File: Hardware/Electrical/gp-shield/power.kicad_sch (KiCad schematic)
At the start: 38 parts, among them J1 XT60/TERM2, J2 XT60/TERM2, Q1 Q_PMOS_GDS, Q2 Q_PMOS_GDS, Q4 Q_PMOS_GDS, SW1 SW_SPDT, U1 NCP1117-5.0_SOT223, U3 LM397, U5 ADCMP350

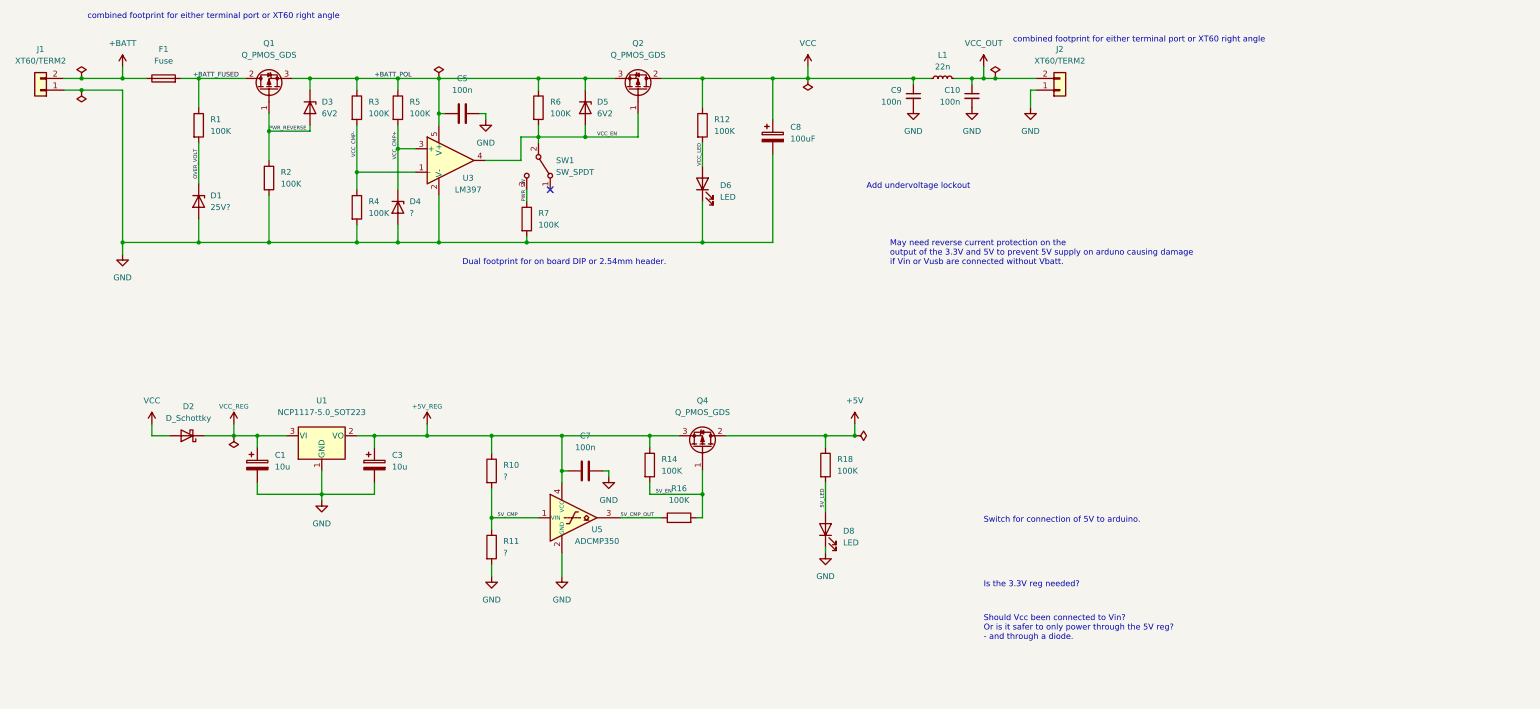
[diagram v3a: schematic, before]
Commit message: Updated Power supply design
Simplified reverse polarity and overvoltage protection
Added adjustable UVLO with precision Vref
Added hysteresis to comparators
Added precision reference to 5V cmp circuit.
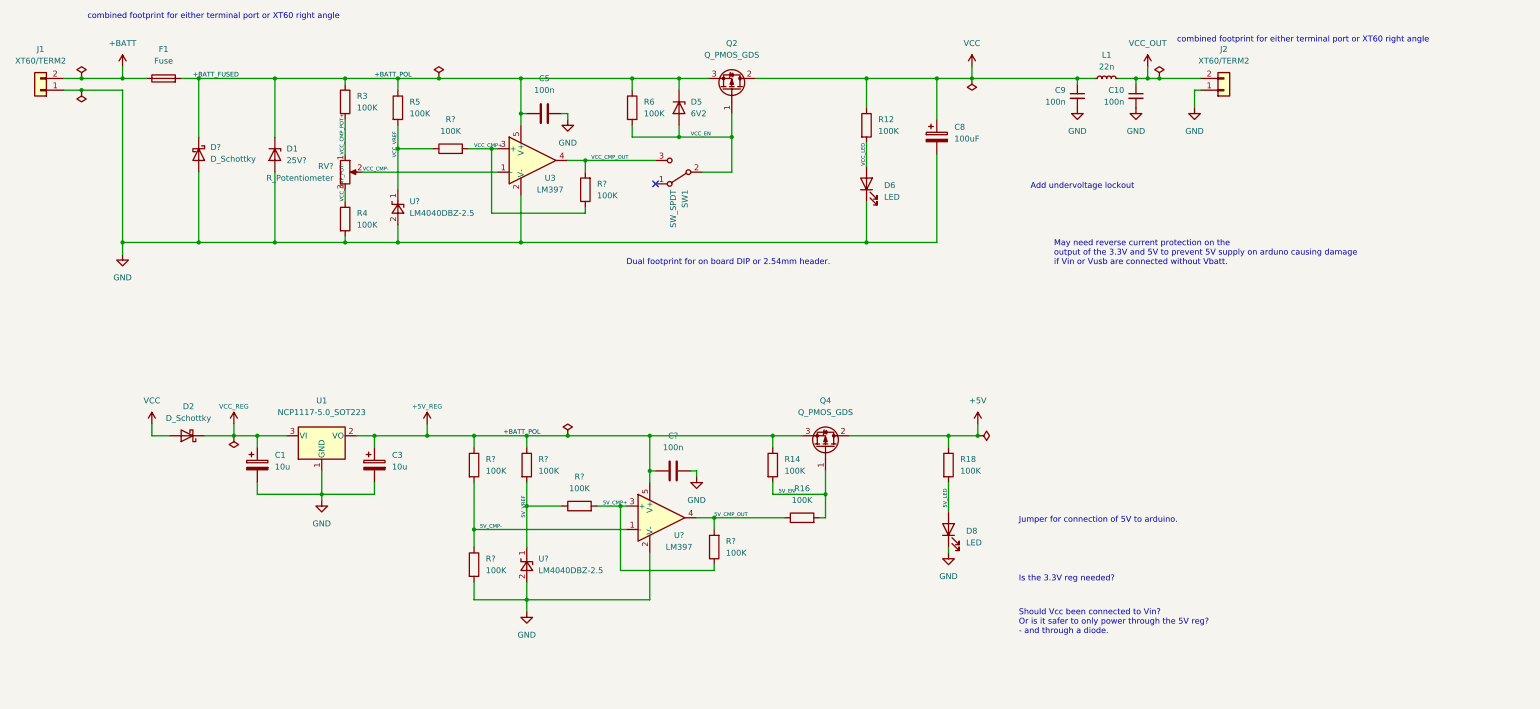
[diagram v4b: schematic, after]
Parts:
- removed C7: 100n, Capacitor_SMD:C_0805_2012Metric_Pad1.18x1.45mm_HandSolder, symbol Device:C
- removed D3: 6V2, Diode_SMD:D_0805_2012Metric_Pad1.15x1.40mm_HandSolder, symbol Device:D_Zener
- removed D4: ?, Diode_SMD:D_0805_2012Metric_Pad1.15x1.40mm_HandSolder, symbol Device:D_Zener
- removed Q1: Q_PMOS_GDS, Package_TO_SOT_SMD:SOT-23, symbol Device:Q_PMOS_GDS
- removed R1, R2, R7: 100K, Resistor_SMD:R_0805_2012Metric_Pad1.20x1.40mm_HandSolder, symbol Device:R
- removed R10, R11: ?, Resistor_SMD:R_0805_2012Metric_Pad1.20x1.40mm_HandSolder, symbol Device:R
- removed U5: ADCMP350, Package_TO_SOT_SMD:Analog_KS-4, symbol Comparator:ADCMP350
- added C?: 100n, Capacitor_SMD:C_0805_2012Metric_Pad1.18x1.45mm_HandSolder, symbol Device:C
- added D?: D_Schottky, symbol Device:D_Schottky
- added R? (x7): 100K, Resistor_SMD:R_0805_2012Metric_Pad1.20x1.40mm_HandSolder, symbol Device:R
- added RV?: R_Potentiometer, symbol Device:R_Potentiometer
- added U?: LM397, Package_TO_SOT_SMD:SOT-23-5, symbol Comparator:LM397
- added U? (x2): LM4040DBZ-2.5, Package_TO_SOT_SMD:SOT-23, symbol Reference_Voltage:LM4040DBZ-2.5
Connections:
- net +BATT_FUSED is gone; now on net +5V_REG: F1.2
- net +BATT_POL is gone; now on net +5V_REG: C5.1, D5.1 (K), Q2.3 (S), R3.1, R5.1, R6.1, U3.5 (V+)
- net OVER_VOLT is gone; now on net +5V_REG: D1.1 (K)
- net +5V_REG: now also C?.1, D?.1 (K), R?.1, R?.1, U?.5 (V+)
- net 5V_CMP_OUT: now also R?.2, U?.4
- net GND: now also C?.2, D?.2 (A), R?.2, U?.2 (A), U?.2 (A), U?.2 (V-)
- net VCC_CMP+: now also R?.1, R?.2; no longer R5.2
- net VCC_CMP-: now also RV?.2; no longer R3.2, R4.1
- net VCC_EN: no longer U3.4
- net PWR_SW renamed VCC_CMP_OUT
- net VCC_CMP_OUT: now also U3.4, R?.2
- new net 5V_CMP+: R?.1, R?.2, U?.3 (+)
- new net 5V_CMP-: R?.1, R?.2, U?.1 (-)
- new net 5V_VREF: R?.1, R?.2, U?.1 (K)
- new net VCC_CMP_POT+: R3.2, RV?.1
- new net VCC_CMP_POT-: R4.1, RV?.3
- new net VCC_VREF: R5.2, R?.1, U?.1 (K)
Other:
- note added: "Jumper for connection of 5V to arduino."
- note removed: "Switch for connection of 5V to arduino."
- moved on the sheet: C10, C5, C8, C9, D1, D5, D6, D8, J2, L1, Q2, Q4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
